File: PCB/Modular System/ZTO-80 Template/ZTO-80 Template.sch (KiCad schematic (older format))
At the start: 4 parts, among them J1 ZTO-80 Bus, J2 Conn_01x02

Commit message: Edited power LED resistor value
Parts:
- R1: value 200 -> 220
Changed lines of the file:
@@
 P 2825 925
 F 0 "R1" V 2725 925 50  0000 C CNN
-F 1 "200" V 2825 925 50  0000 C CNN
+F 1 "220" V 2825 925 50  0000 C CNN
 F 2 "Resistor_SMD:R_0805_2012Metric_Pad1.15x1.40mm_HandSolder" V 2755 925 50  0001 C CNN
 F 3 "~" H 2825 925 50  0001 C CNN

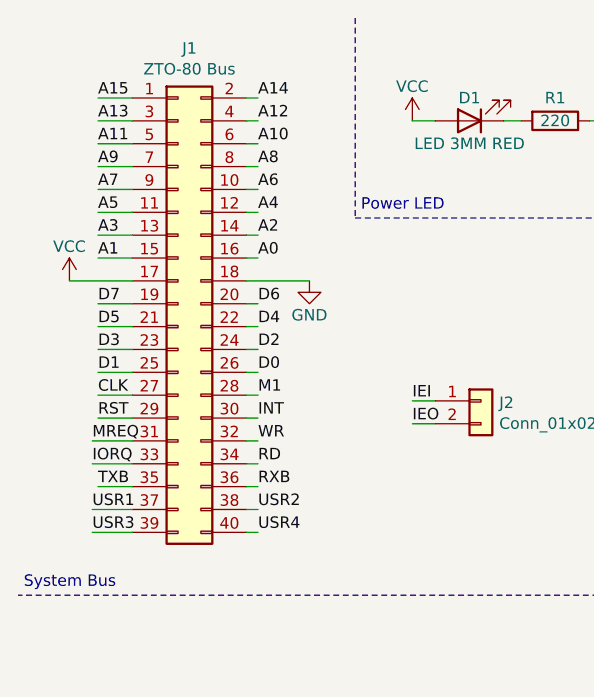
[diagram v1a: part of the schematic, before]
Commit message: Changed bus orientation
This change is backwards-compatible with all previous ZTO-80 modules
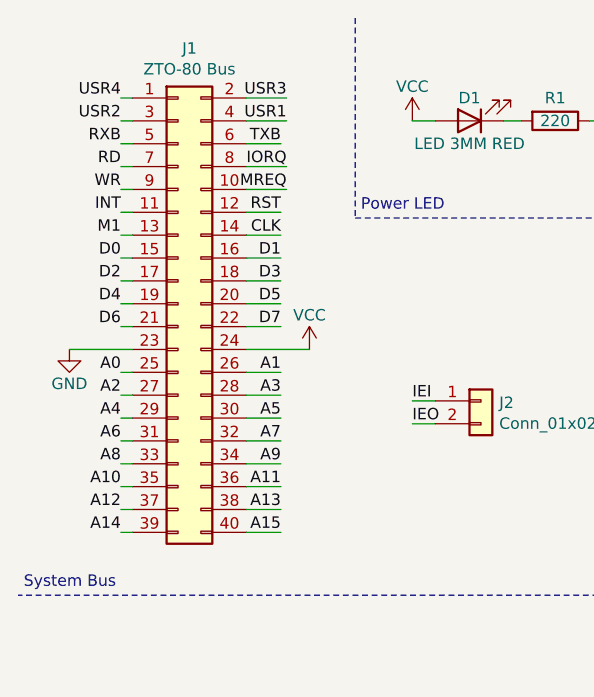
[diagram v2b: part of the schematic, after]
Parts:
- J1: footprint ZTO-80_Header:PinHeader_2x20_P2.54mm_Horizontal -> Connector_PinHeader_2.54mm:PinHeader_2x20_P2.54mm_Horizontal
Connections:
- net A0: now also J1.25 (Pin_25); no longer J1.16 (Pin_16)
- net A1: now also J1.26 (Pin_26); no longer J1.15 (Pin_15)
- net A10: now also J1.35 (Pin_35); no longer J1.6 (Pin_6)
- net A11: now also J1.36 (Pin_36); no longer J1.5 (Pin_5)
- net A12: now also J1.37 (Pin_37); no longer J1.4 (Pin_4)
- net A13: now also J1.38 (Pin_38); no longer J1.3 (Pin_3)
- net A14: now also J1.39 (Pin_39); no longer J1.2 (Pin_2)
- net A15: now also J1.40 (Pin_40); no longer J1.1 (Pin_1)
- net A2: now also J1.27 (Pin_27); no longer J1.14 (Pin_14)
- net A3: now also J1.28 (Pin_28); no longer J1.13 (Pin_13)
- net A4: now also J1.29 (Pin_29); no longer J1.12 (Pin_12)
- net A5: now also J1.30 (Pin_30); no longer J1.11 (Pin_11)
- net A6: now also J1.31 (Pin_31); no longer J1.10 (Pin_10)
- net A7: now also J1.32 (Pin_32); no longer J1.9 (Pin_9)
- net A8: now also J1.33 (Pin_33); no longer J1.8 (Pin_8)
- net A9: now also J1.34 (Pin_34); no longer J1.7 (Pin_7)
- net CLK: now also J1.14 (Pin_14); no longer J1.27 (Pin_27)
- net D0: now also J1.15 (Pin_15); no longer J1.26 (Pin_26)
- net D1: now also J1.16 (Pin_16); no longer J1.25 (Pin_25)
- net D2: now also J1.17 (Pin_17); no longer J1.24 (Pin_24)
- net D3: now also J1.18 (Pin_18); no longer J1.23 (Pin_23)
- net D4: now also J1.19 (Pin_19); no longer J1.22 (Pin_22)
- net D5: now also J1.20 (Pin_20); no longer J1.21 (Pin_21)
- net D6: now also J1.21 (Pin_21); no longer J1.20 (Pin_20)
- net D7: now also J1.22 (Pin_22); no longer J1.19 (Pin_19)
- net GND: now also J1.23 (Pin_23); no longer J1.18 (Pin_18)
- net INT: now also J1.11 (Pin_11); no longer J1.30 (Pin_30)
- net IORQ: now also J1.8 (Pin_8); no longer J1.33 (Pin_33)
- net M1: now also J1.13 (Pin_13); no longer J1.28 (Pin_28)
- net MREQ: now also J1.10 (Pin_10); no longer J1.31 (Pin_31)
- net RD: now also J1.7 (Pin_7); no longer J1.34 (Pin_34)
- net RST: now also J1.12 (Pin_12); no longer J1.29 (Pin_29)
- net RXB: now also J1.5 (Pin_5); no longer J1.36 (Pin_36)
- net TXB: now also J1.6 (Pin_6); no longer J1.35 (Pin_35)
- net USR1: now also J1.4 (Pin_4); no longer J1.37 (Pin_37)
- net USR2: now also J1.3 (Pin_3); no longer J1.38 (Pin_38)
- net USR3: now also J1.2 (Pin_2); no longer J1.39 (Pin_39)
- net USR4: now also J1.1 (Pin_1); no longer J1.40 (Pin_40)
- net VCC: now also J1.24 (Pin_24); no longer J1.17 (Pin_17)
- net WR: now also J1.9 (Pin_9); no longer J1.32 (Pin_32)
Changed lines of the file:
@@
 	3350 3000 3350 475
 Wire Wire Line
-	825  2525 975  2525
+	1625 1025 1475 1025
 Wire Wire Line
-	800  2625 975  2625
+	1650 925  1475 925
 Wire Wire Line
-	800  2725 975  2725
+	1650 825  1475 825
+Wire Wire Line
+	1475 2725 1625 2725
+Wire Wire Line
+	1475 2625 1625 2625
+Wire Wire Line
+	1475 2525 1625 2525
+Wire Wire Line
+	1475 2425 1625 2425
+Wire Wire Line
+	1475 2325 1625 2325
+Wire Wire Line
+	1475 2225 1625 2225
+Wire Wire Line
+	1475 2125 1625 2125
+Wire Wire Line
+	1475 2025 1625 2025
+Wire Wire Line
+	1475 1825 1625 1825
+Wire Wire Line
+	1475 1725 1625 1725
+Wire Wire Line
+	1475 1625 1625 1625
+Wire Wire Line
+	1475 1525 1625 1525
+Wire Wire Line
+	1475 1425 1625 1425
+Wire Wire Line
+	1475 1325 1625 1325
+Text Label 925  2025 2    50   ~ 0
+A0
+Text Label 1625 2025 2    50   ~ 0
+A1
+Text Label 925  2125 2    50   ~ 0
+A2
+Text Label 1625 2125 2    50   ~ 0
+A3
+Text Label 925  2225 2    50   ~ 0
+A4
+Text Label 1625 2225 2    50   ~ 0
+A5
+Text Label 925  2325 2    50   ~ 0
+A6
+Text Label 1625 2325 2    50   ~ 0
+A7
+Text Label 925  2425 2    50   ~ 0
+A8
+Text Label 1625 2425 2    50   ~ 0
+A9
+Text Label 925  2525 2    50   ~ 0
+A10
+Text Label 1625 2525 2    50   ~ 0
+A11
+Text Label 925  2625 2    50   ~ 0
+A12
+Text Label 1625 2625 2    50   ~ 0
+A13
+Text Label 925  2725 2    50   ~ 0
+A14
+Text Label 1625 2725 2    50   ~ 0
+A15
+$Comp
+L power:VCC #PWR01
+U 1 1 5E287266
+P 1750 1925
+F 0 "#PWR01" H 1750 1775 50  0001 C CNN
+F 1 "VCC" H 1750 2075 50  0000 C CNN
+F 2 "" H 1750 1925 50  0001 C CNN
+F 3 "" H 1750 1925 50  0001 C CNN
+	1    1750 1925
+	1    0    0    -1
+$EndComp
+Wire Wire Line
+	1750 1925 1475 1925
+$Comp
+L power:GND #PWR02
+U 1 1 5E288EF4
+P 700 1925
+F 0 "#PWR02" H 700 1675 50  0001 C CNN
+F 1 "GND" H 700 1775 50  0000 C CNN
+F 2 "" H 700 1925 50  0001 C CNN
+F 3 "" H 700 1925 50  0001 C CNN
+	1    700  1925
+	1    0    0    -1
+$EndComp
+Wire Wire Line
+	975  2725 925  2725
+Wire Wire Line
+	975  2625 925  2625
+Wire Wire Line
+	975  2525 925  2525
+Wire Wire Line
+	975  2425 925  2425
+Wire Wire Line
+	975  2325 925  2325
+Wire Wire Line
+	975  2225 925  2225
+Wire Wire Line
+	975  2125 925  2125
+Wire Wire Line
+	975  2025 925  2025
+Wire Wire Line
+	975  1825 925  1825
+Wire Wire Line
+	975  1725 925  1725
+Wire Wire Line
+	975  1625 925  1625
+Wire Wire Line
+	975  1525 925  1525
+Wire Wire Line
+	975  1425 925  1425
+Wire Wire Line
+	975  1325 925  1325
+Wire Wire Line
+	975  1225 925  1225
+Wire Wire Line
+	975  1125 925  1125
+Wire Wire Line
+	975  1025 925  1025
+Wire Wire Line
+	975  925  925  925
+Wire Wire Line
+	975  825  925  825
+Wire Wire Line
+	975  1925 700  1925
+Text Label 1625 1525 2    50   ~ 0
+D1
+Text Label 925  1625 2    50   ~ 0
+D2
+Text Label 1625 1625 2    50   ~ 0
+D3
+Text Label 925  1725 2    50   ~ 0
+D4
+Text Label 925  1825 2    50   ~ 0
+D6
+Text Label 1625 1825 2    50   ~ 0
+D7
+Text Label 925  1525 2    50   ~ 0
+D0
+Text Label 1625 1725 2    50   ~ 0
+D5
+Text Label 1625 1425 2    50   ~ 0
+CLK
+Text Label 925  1425 2    50   ~ 0
+M1
+Text Label 1625 1325 2    50   ~ 0
+RST
+Text Label 925  1325 2    50   ~ 0
+INT
+Text Label 1650 1225 2    50   ~ 0
+MREQ
+Wire Wire Line
+	1650 1225 1475 1225
+Text Label 925  1225 2    50   ~ 0
+WR
+Text Label 1650 1125 2    50   ~ 0
+IORQ
+Wire Wire Line
+	1650 1125 1475 1125
+Text Label 925  1125 2    50   ~ 0
+RD
+Text Label 1625 1025 2    50   ~ 0
+TXB
+Text Label 925  1025 2    50   ~ 0
+RXB
+Text Label 925  925  2    50   ~ 0
+USR2
+Text Label 1650 825  2    50   ~ 0
+USR3
+Text Label 925  825  2    50   ~ 0
+USR4
+Text Label 1650 925  2    50   ~ 0
+USR1
 $Comp
 L Connector_Generic:Conn_02x20_Odd_Even J1
-U 1 1 5E25F961
+U 1 1 5F3B76C7
 P 1175 1725
 F 0 "J1" H 1225 2842 50  0000 C CNN
 F 1 "ZTO-80 Bus" H 1225 2751 50  0000 C CNN
-F 2 "ZTO-80_Header:PinHeader_2x20_P2.54mm_Horizontal" H 1175 1725 50  0001 C CNN
+F 2 "Connector_PinHeader_2.54mm:PinHeader_2x20_P2.54mm_Horizontal" H 1175 1725 50  0001 C CNN
 F 3 "~" H 1175 1725 50  0001 C CNN
 	1    1175 1725
 	1    0    0    -1
 $EndComp
-Wire Wire Line
-	975  825  825  825
-Wire Wire Line
-	975  925  825  925
-Wire Wire Line
-	975  1025 825  1025
-Wire Wire Line
-	975  1125 825  1125
-Wire Wire Line
-	975  1225 825  1225
-Wire Wire Line
-	975  1325 825  1325
-Wire Wire Line
-	975  1425 825  1425
-Wire Wire Line
-	975  1525 825  1525
-Wire Wire Line
-	975  1725 825  1725
-Wire Wire Line
-	975  1825 825  1825
-Wire Wire Line
-	975  1925 825  1925
-Wire Wire Line
-	975  2025 825  2025
-Wire Wire Line
-	975  2125 825  2125
-Wire Wire Line
-	975  2225 825  2225
-Text Label 1525 1525 0    50   ~ 0
-A0
-Text Label 825  1525 0    50   ~ 0
-A1
-Text Label 1525 1425 0    50   ~ 0
-A2
-Text Label 825  1425 0    50   ~ 0
-A3
-Text Label 1525 1325 0    50   ~ 0
-A4
-Text Label 825  1325 0    50   ~ 0
-A5
-Text Label 1525 1225 0    50   ~ 0
-A6
-Text Label 825  1225 0    50   ~ 0
-A7
-Text Label 1525 1125 0    50   ~ 0
-A8
-Text Label 825  1125 0    50   ~ 0
-A9
-Text Label 1525 1025 0    50   ~ 0
-A10
-Text Label 825  1025 0    50   ~ 0
-A11
-Text Label 1525 925  0    50   ~ 0
-A12
-Text Label 825  925  0    50   ~ 0
-A13
-Text Label 1525 825  0    50   ~ 0
-A14
-Text Label 825  825  0    50   ~ 0
-A15
-$Comp
-L power:VCC #PWR01
-U 1 1 5E287266
-P 700 1625
-F 0 "#PWR01" H 700 1475 50  0001 C CNN
-F 1 "VCC" H 700 1775 50  0000 C CNN
-F 2 "" H 700 1625 50  0001 C CNN
-F 3 "" H 700 1625 50  0001 C CNN
-	1    700  1625
-	1    0    0    -1
-$EndComp
-Wire Wire Line
-	700  1625 975  1625
-$Comp
-L power:GND #PWR02
-U 1 1 5E288EF4
-P 1750 1625
-F 0 "#PWR02" H 1750 1375 50  0001 C CNN
-F 1 "GND" H 1750 1475 50  0000 C CNN
-F 2 "" H 1750 1625 50  0001 C CNN
-F 3 "" H 1750 1625 50  0001 C CNN
-	1    1750 1625
-	1    0    0    -1
-$EndComp
-Wire Wire Line
-	1475 825  1525 825
-Wire Wire Line
-	1475 925  1525 925
-Wire Wire Line
-	1475 1025 1525 1025
-Wire Wire Line
-	1475 1125 1525 1125
-Wire Wire Line
-	1475 1225 1525 1225
-Wire Wire Line
-	1475 1325 1525 1325
-Wire Wire Line
-	1475 1425 1525 1425
-Wire Wire Line
-	1475 1525 1525 1525
-Wire Wire Line
-	1475 1725 1525 1725
-Wire Wire Line
-	1475 1825 1525 1825
-Wire Wire Line
-	1475 1925 1525 1925
-Wire Wire Line
-	1475 2025 1525 2025
-Wire Wire Line
-	1475 2125 1525 2125
-Wire Wire Line
-	1475 2225 1525 2225
-Wire Wire Line
-	1475 2325 1525 2325
-Wire Wire Line
-	1475 2425 1525 2425
-Wire Wire Line
-	1475 2525 1525 2525
-Wire Wire Line
-	1475 2625 1525 2625
-Wire Wire Line
-	1475 2725 1525 2725
-Wire Wire Line
-	1475 1625 1750 1625
-Text Label 825  2025 0    50   ~ 0
-D1
-Text Label 1525 1925 0    50   ~ 0
-D2
-Text Label 825  1925 0    50   ~ 0
-D3
-Text Label 1525 1825 0    50   ~ 0
-D4
-Text Label 1525 1725 0    50   ~ 0
-D6
-Text Label 825  1725 0    50   ~ 0
-D7
-Text Label 1525 2025 0    50   ~ 0
-D0
-Text Label 825  1825 0    50   ~ 0
-D5
-Text Label 825  2125 0    50   ~ 0
-CLK
-Text Label 1525 2125 0    50   ~ 0
-M1
-Text Label 825  2225 0    50   ~ 0
-RST
-Text Label 1525 2225 0    50   ~ 0
-INT
-Text Label 800  2325 0    50   ~ 0
-MREQ
-Wire Wire Line
-	800  2325 975  2325
-Text Label 1525 2325 0    50   ~ 0
-WR
-Text Label 800  2425 0    50   ~ 0
-IORQ
-Wire Wire Line
-	800  2425 975  2425
-Text Label 1525 2425 0    50   ~ 0
-RD
-Text Label 825  2525 0    50   ~ 0
-TXB
-Text Label 1525 2525 0    50   ~ 0
-RXB
-Text Label 1525 2625 0    50   ~ 0
-USR2
-Text Label 800  2725 0    50   ~ 0
-USR3
-Text Label 1525 2725 0    50   ~ 0
-USR4
-Text Label 800  2625 0    50   ~ 0
-USR1
 $EndSCHEMATC
